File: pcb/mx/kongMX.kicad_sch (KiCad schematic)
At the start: 129 parts, among them J500 USB_C_Receptacle_USB2.0, J501 BL_CONN, SW500 SW_Push, SW501 SW_Push, SW502 SW_Push, SW503 SW_Push, SW504 SW_Push, SW505 SW_Push, SW506 SW_Push, SW507 SW_Push, SW508 SW_Push, SW509 SW_Push, SW510 SW_Push, SW511 SW_Push, SW512 SW_Push, SW513 SW_Push, SW514 SW_Push, SW515 SW_Push, SW516 SW_Push, SW517 SW_Push, SW518 SW_Push, SW519 SW_Push, SW520 SW_Push, SW521 SW_Push, SW522 SW_Push, SW523 SW_Push, SW524 SW_Push, SW525 SW_Push, SW526 SW_Push, SW527 SW_Push, SW528 SW_Push, SW529 SW_Push, SW530 SW_Push, SW531 SW_Push, SW532 SW_Push, SW533 SW_Push, SW534 SW_Push, SW535 SW_Push, SW536 SW_Push, SW537 SW_Push, SW538 SW_Push, SW539 SW_Push, SW540 SW_Push, SW541 SW_Push, SW542 SW_Push, SW543 SW_Push, SW544 SW_Push, SW545 SW_Push, SW546 SW_Push, SW547 SW_Push, SW548 SW_Push, SW549 SW_Push, SW550 SW_Push, SW551 SW_Push, U500 XC6206PxxxMR, U501 USBLC6-2SC6, U502 W25Q128JVS, U503 RP2040, Y500 Crystal_GND24_Small

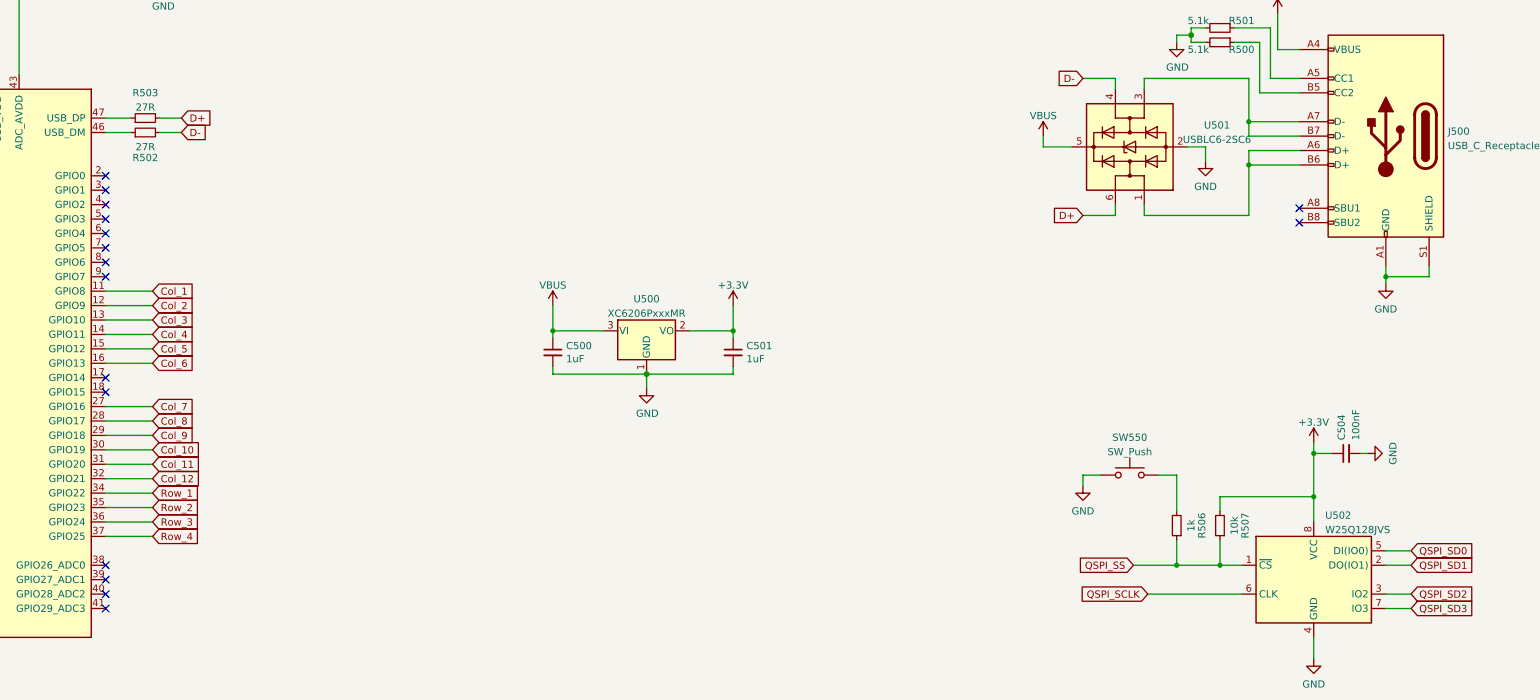
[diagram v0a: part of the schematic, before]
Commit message: added i2c breakout header to pcb
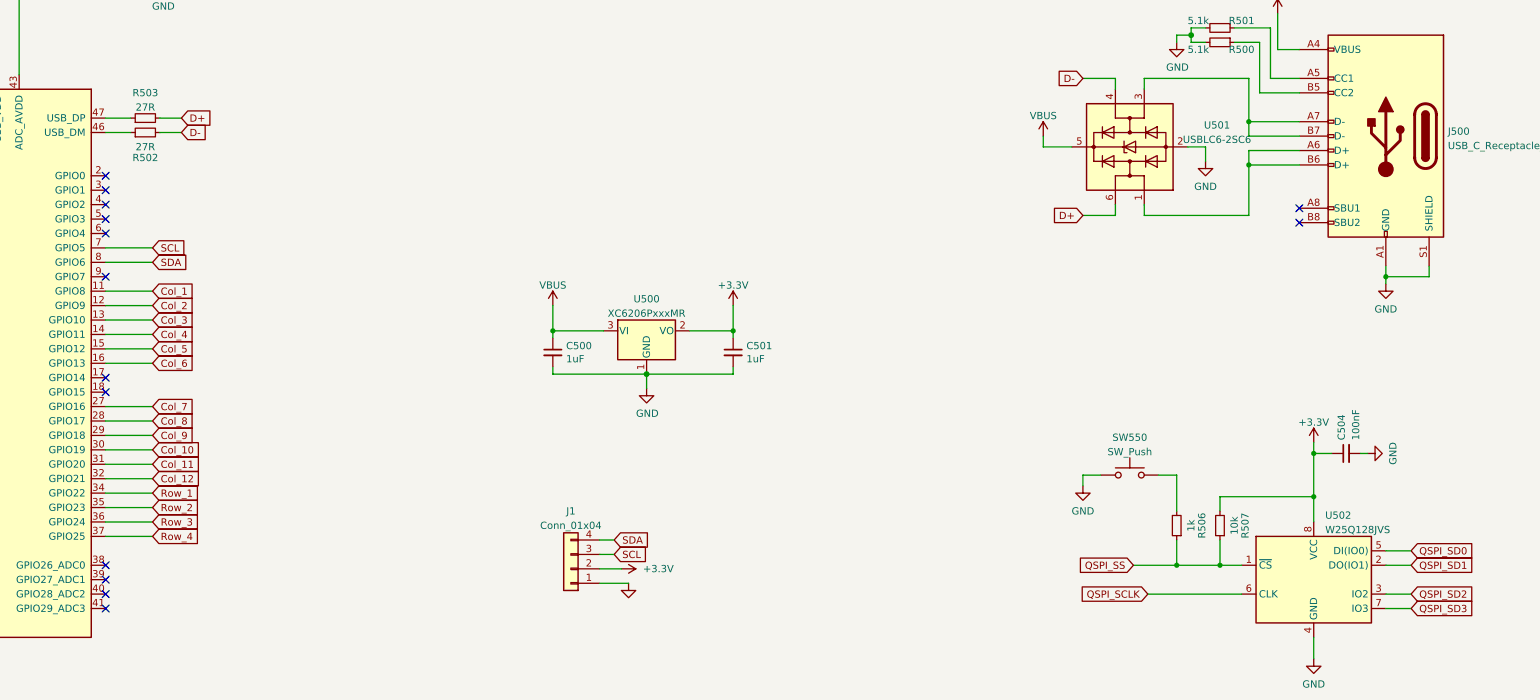
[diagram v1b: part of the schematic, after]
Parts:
- added J1: Conn_01x04, Connector_PinHeader_2.54mm:PinHeader_1x04_P2.54mm_Vertical, symbol Connector_Generic:Conn_01x04
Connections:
- net +3.3V: now also J1.2 (Pin_2)
- net GND: now also J1.1 (Pin_1)
- net SCL: now reaches U503.7 (GPIO5)
- net SCL: now also J1.3 (Pin_3)
- net SDA: now reaches U503.8 (GPIO6)
- net SDA: now also J1.4 (Pin_4)
- no-connect marks 16 -> 14
